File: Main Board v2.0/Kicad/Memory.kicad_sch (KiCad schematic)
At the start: 0 parts

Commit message: update
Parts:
- added C3, C4, C5, C6, C7: 100n, symbol Device:C
- added R1, R2, R3, R4, R5: 10k, symbol Device:R_Small
- added U10, U11, U12, U?: UM61512A, Footprints:DIP-32_0_ELL, symbol Z80-CPU-Board-rescue:UM61512A
- added U9: AM29F040B, Package_DIP:DIP-32_W15.24mm, symbol Memory_RAM:AS6C4008-55PCN
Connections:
- new net: R3.1, U10.30 (CE2)
- new net: R1.1, U?.30 (CE2)
- new net: R5.1, U12.30 (CE2)
- new net: R2.1, U9.31 (WE#)
- new net: R4.1, U11.30 (CE2)
- new net +5V: C3.1, C4.1, C5.1, C6.1, C7.1, R1.2, R2.2, R3.2, R4.2, R5.2, U10.32 (VCC), U11.32 (VCC), U12.32 (VCC), U9.32 (VCC), U?.32 (VCC)
- new net D0: U10.13 (D0), U11.13 (D0), U12.13 (D0), U9.13 (DQ0), U?.13 (D0)
- new net D1: U10.14 (D1), U11.14 (D1), U12.14 (D1), U9.14 (DQ1), U?.14 (D1)
- new net D2: U10.15 (D2), U11.15 (D2), U12.15 (D2), U9.15 (DQ2), U?.15 (D2)
- new net D3: U10.17 (D3), U11.17 (D3), U12.17 (D3), U9.17 (DQ3), U?.17 (D3)
- new net D4: U10.18 (D4), U11.18 (D4), U12.18 (D4), U9.18 (DQ4), U?.18 (D4)
- new net D5: U10.19 (D5), U11.19 (D5), U12.19 (D5), U9.19 (DQ5), U?.19 (D5)
- new net D6: U10.20 (D6), U11.20 (D6), U12.20 (D6), U9.20 (DQ6), U?.20 (D6)
- new net D7: U10.21 (D7), U11.21 (D7), U12.21 (D7), U9.21 (DQ7), U?.21 (D7)
- new net GND: C3.2, C4.2, C5.2, C6.2, C7.2, U10.16 (GND), U11.16 (GND), U12.16 (GND), U9.16 (VSS), U?.16 (GND)
- new net MA0: U10.12 (A0), U11.12 (A0), U12.12 (A0), U9.12 (A0), U?.12 (A0)
- new net MA1: U10.11 (A1), U11.11 (A1), U12.11 (A1), U9.11 (A1), U?.11 (A1)
- new net MA10: U10.23 (A10), U11.23 (A10), U12.23 (A10), U9.23 (A10), U?.23 (A10)
- new net MA11: U10.25 (A11), U11.25 (A11), U12.25 (A11), U9.25 (A11), U?.25 (A11)
- new net MA12: U10.4 (A12), U11.4 (A12), U12.4 (A12), U9.4 (A12), U?.4 (A12)
- new net MA13: U10.28 (A13), U11.28 (A13), U12.28 (A13), U9.28 (A13), U?.28 (A13)
- new net MA14: U10.3 (A14), U11.3 (A14), U12.3 (A14), U?.3 (A14)
- new net MA15: U10.31 (A15), U11.31 (A15), U12.31 (A15), U?.31 (A15)
- new net MA2: U10.10 (A2), U11.10 (A2), U12.10 (A2), U9.10 (A2), U?.10 (A2)
- new net MA3: U10.9 (A3), U11.9 (A3), U12.9 (A3), U9.9 (A3), U?.9 (A3)
- new net MA4: U10.8 (A4), U11.8 (A4), U12.8 (A4), U9.8 (A4), U?.8 (A4)
- new net MA5: U10.7 (A5), U11.7 (A5), U12.7 (A5), U9.7 (A5), U?.7 (A5)
- new net MA6: U10.6 (A6), U11.6 (A6), U12.6 (A6), U9.6 (A6), U?.6 (A6)
- new net MA7: U10.5 (A7), U11.5 (A7), U12.5 (A7), U9.5 (A7), U?.5 (A7)
- new net MA8: U10.27 (A8), U11.27 (A8), U12.27 (A8), U9.27 (A8), U?.27 (A8)
- new net MA9: U10.26 (A9), U11.26 (A9), U12.26 (A9), U9.26 (A9), U?.26 (A9)
- new net MROM_SEL0: U9.29 (A14)
- new net MROM_SEL1: U9.3 (A15)
- new net MROM_SEL2: U9.2 (A16)
- new net MROM_SEL3: U9.30 (A17)
- new net MROM_SEL4: U9.1 (A18)
- new net ~{ME0}: U9.22 (CE#)
- new net ~{ME1}: U11.22 (CE1)
- new net ~{ME2}: U?.22 (CE1)
- new net ~{ME3}: U10.22 (CE1)
- new net ~{ME4}: U12.22 (CE1)
- new net ~{RD}: U10.24 (OE), U11.24 (OE), U12.24 (OE), U9.24 (OE#), U?.24 (OE)
- new net ~{WR}: U10.29 (WR), U11.29 (WR), U12.29 (WR), U?.29 (WR)
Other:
- note added: "ROM has 32x 16k pages."
- note added: "ZIF socket"

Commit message: schematic done*
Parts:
- removed C5, C6, C7: 100n, symbol Device:C
- removed R1, R2, R3, R4, R5: 10k, symbol Device:R_Small
- removed U10, U11, U12, U?: UM61512A, Footprints:DIP-32_0_ELL, symbol Z80-CPU-Board-rescue:UM61512A
- added U5: AS6C4008-55PCN, Package_SO:SOP-32_11.305x20.495mm_P1.27mm, symbol Memory_RAM:AS6C4008-55PCN
- C7: renamed from C3; footprint (none) -> Capacitor_SMD:C_0603_1608Metric_Pad1.08x0.95mm_HandSolder
- C8: renamed from C4; footprint (none) -> Capacitor_SMD:C_0603_1608Metric_Pad1.08x0.95mm_HandSolder
- U6: renamed from U9; footprint Package_DIP:DIP-32_W15.24mm -> Socket:3M_Textool_240-1288-00-0602J_2x20_P2.54mm
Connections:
- net MROM_SEL0 is gone; now on net MA14: U6.29 (A14)
- net MROM_SEL1 is gone; now on net MA15: U6.3 (A15)
- net MROM_SEL2 is gone; now on net MA16: U6.2 (A16)
- net MROM_SEL3 is gone; now on net MA17: U6.30 (A17)
- net MROM_SEL4 is gone; now on net MA18: U6.1 (A18)
- net +5V: now also U5.32 (VCC)
- net D0: now also U5.13 (DQ0)
- net D1: now also U5.14 (DQ1)
- net D2: now also U5.15 (DQ2)
- net D3: now also U5.17 (DQ3)
- net D4: now also U5.18 (DQ4)
- net D5: now also U5.19 (DQ5)
- net D6: now also U5.20 (DQ6)
- net D7: now also U5.21 (DQ7)
- net GND: now also U5.16 (VSS)
- net MA13: now also U5.28 (A13)
- net MA14: now also U5.3 (A14)
- net MA15: now also U5.31 (A15)
- net MA16: now also U5.2 (A16)
- net MA17: now also U5.30 (A17)
- net MA18: now also U5.1 (A18)
- net ROM_WE#: now reaches U6.31 (WE#)
- net MA0 renamed A0
- net A0: now also U5.12 (A0)
- net MA1 renamed A1
- net A1: now also U5.11 (A1)
- net MA10 renamed A10
- net A10: now also U5.23 (A10)
- net MA11 renamed A11
- net A11: now also U5.25 (A11)
- net MA12 renamed A12
- net A12: now also U5.4 (A12)
- net MA2 renamed A2
- net A2: now also U5.10 (A2)
- net MA3 renamed A3
- net A3: now also U5.9 (A3)
- net MA4 renamed A4
- net A4: now also U5.8 (A4)
- net MA5 renamed A5
- net A5: now also U5.7 (A5)
- net MA6 renamed A6
- net A6: now also U5.6 (A6)
- net MA7 renamed A7
- net A7: now also U5.5 (A7)
- net MA8 renamed A8
- net A8: now also U5.27 (A8)
- net MA9 renamed A9
- net A9: now also U5.26 (A9)
- net ~{ME0} renamed ~{ROM_CE}
- net ~{RD} renamed ~{CPU_RD}
- net ~{CPU_RD}: now also U5.24 (OE#)
- new net ~{CPU_WR}: U5.29 (WE#)
- new net ~{RAM_CE}: U5.22 (CE#)
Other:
- note added: "To CPU Sheet"
- note added: "ZIF32 socket"
- note removed: "ROM has 32x 16k pages."
- note removed: "ZIF socket"
- moved on the sheet: U6

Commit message: board update
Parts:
- U6: footprint Socket:3M_Textool_240-1288-00-0602J_2x20_P2.54mm -> Socket:3M_Textool_232-1288-00-0602J_2x16_P2.54mm
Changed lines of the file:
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@@
 	)
 	(hierarchical_label "A[0..15]"
-		(shape input)
+		(shape tri_state)
 		(at 25.4 125.73 180)
 		(effects
@@
 			)
 		)
-		(property "Footprint" "Socket:3M_Textool_240-1288-00-0602J_2x20_P2.54mm"
+		(property "Footprint" "Socket:3M_Textool_232-1288-00-0602J_2x16_P2.54mm"
 			(at 176.53 62.23 0)
 			(hide yes)

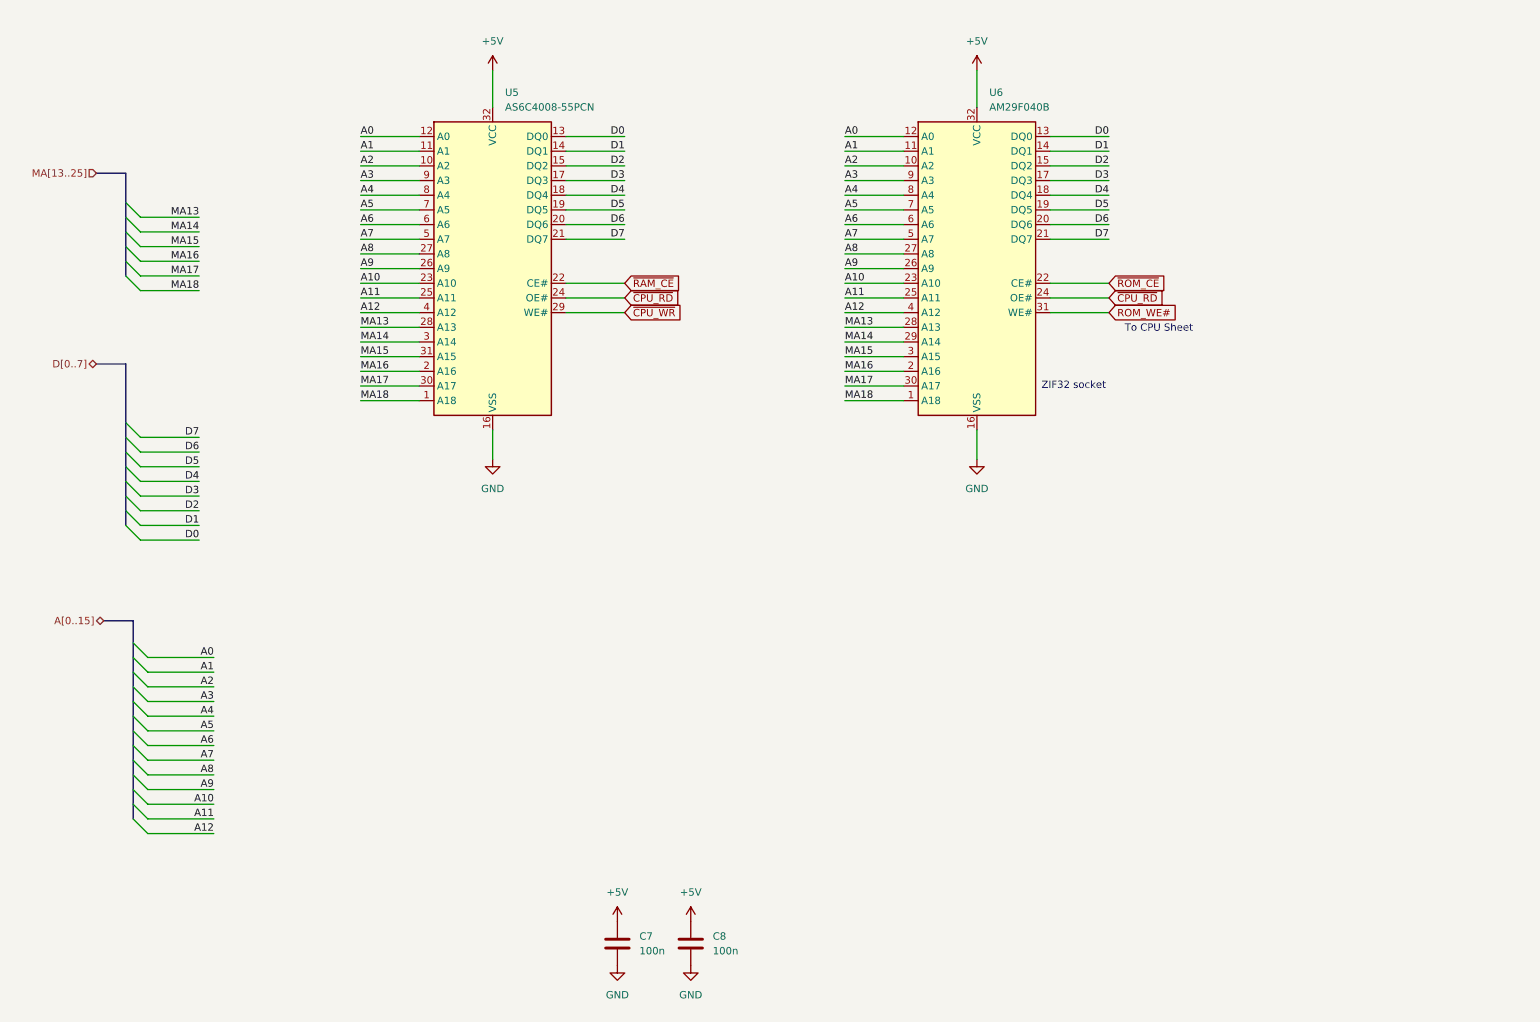
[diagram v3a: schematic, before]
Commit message: schematic update
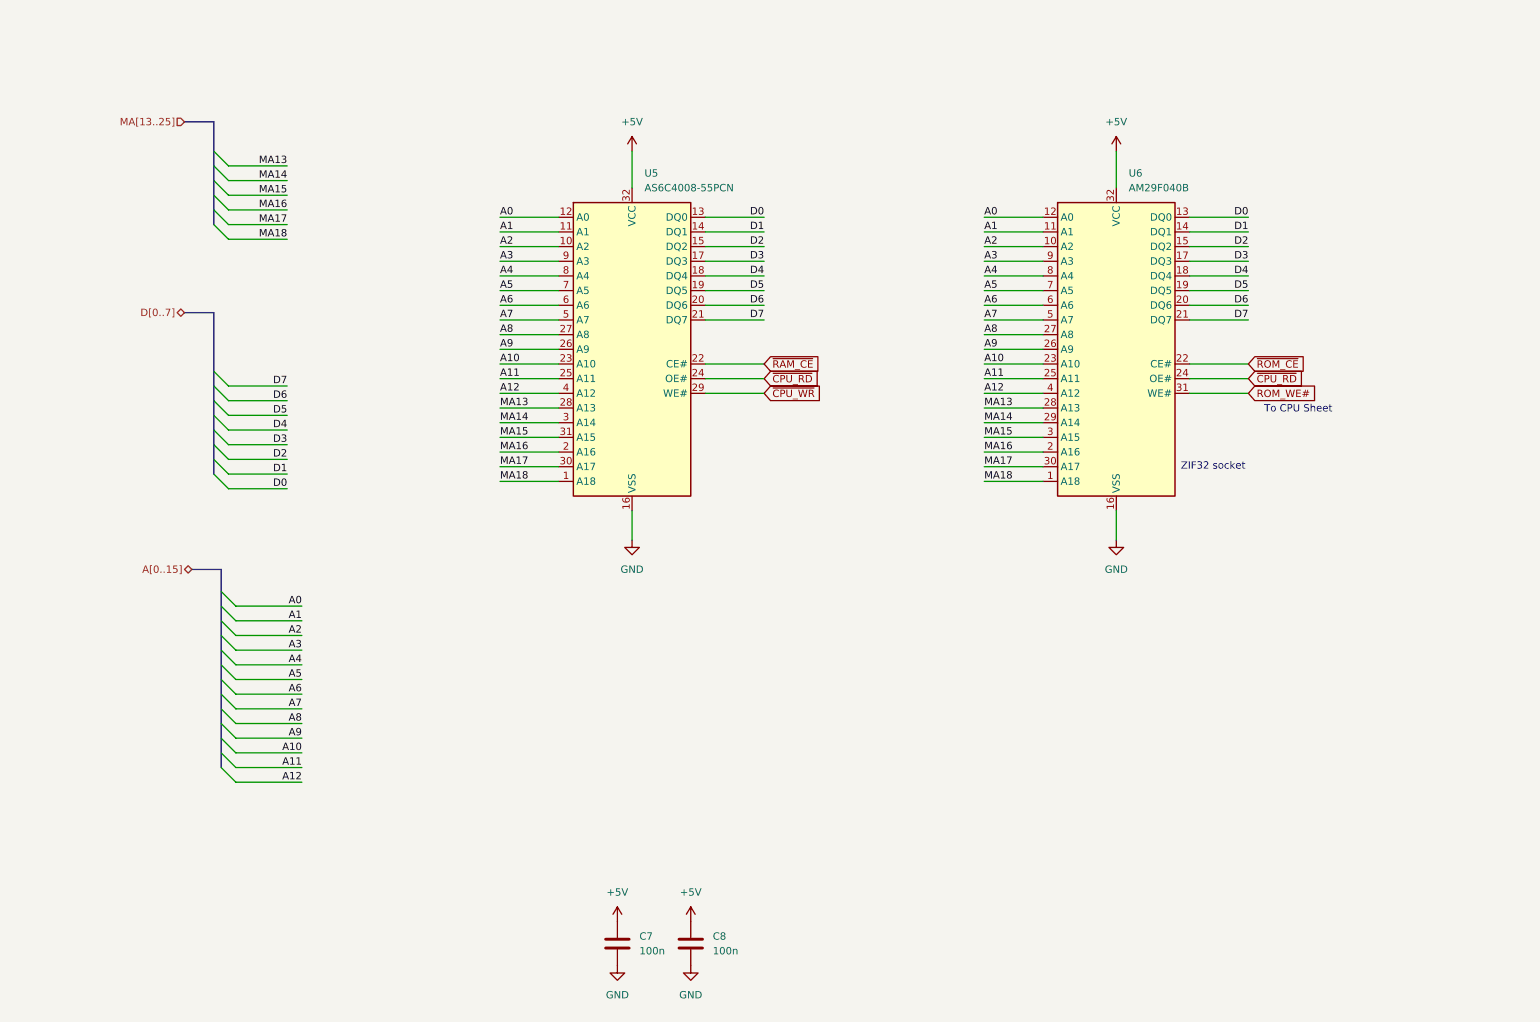
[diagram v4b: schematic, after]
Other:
- moved on the sheet: U5, U6

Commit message: schematic updates
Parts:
- added R27: 10k, Resistor_SMD:R_0603_1608Metric_Pad0.98x0.95mm_HandSolder, symbol Device:R_Small
- renumbered C7 to C5, C8 to C6
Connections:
- net +5V: now also R27.1
- net ROM_WE#: no longer names the net of U6.31 (WE#)
- net ROM_WE#: now also R27.2
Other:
- note removed: "To CPU Sheet"
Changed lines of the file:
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@@
 	(generator_version "10.0")
 	(paper "A4")
-	(text "To CPU Sheet"
-		(exclude_from_sim no)
-		(at 232.156 89.154 0)
-		(effects
-			(font
-				(size 1.27 1.27)
-			)
-		)
-	)
 	(text "ZIF32 socket"
 		(exclude_from_sim no)
@@
 		)
 	)
+	(wire
+		(pts
+			(xy 243.84 77.47) (xy 243.84 80.01)
+		)
+		(stroke
+			(width 0)
+			(type default)
+		)
+	)
 	(bus
 		(pts
@@
 	(wire
 		(pts
+			(xy 243.84 86.36) (xy 243.84 85.09)
+		)
+		(stroke
+			(width 0)
+			(type default)
+		)
+	)
+	(wire
+		(pts
 			(xy 48.26 148.59) (xy 59.69 148.59)
 		)
@@
 	(wire
 		(pts
-			(xy 213.36 86.36) (xy 223.52 86.36)
+			(xy 213.36 86.36) (xy 243.84 86.36)
 		)
 		(stroke
@@
 		(property "Intersheetrefs" "${INTERSHEET_REFS}"
 			(at 150.2447 86.36 0)
-			(hide yes)
-			(show_name no)
-			(do_not_autoplace no)
-			(effects
-				(font
-					(size 1.27 1.27)
-				)
-				(justify left)
-			)
-		)
-	)
-	(global_label "ROM_WE#"
-		(shape input)
-		(at 223.52 86.36 0)
-		(fields_autoplaced yes)
-		(effects
-			(font
-				(size 1.27 1.27)
-			)
-			(justify left)
-		)
-		(property "Intersheetrefs" "${INTERSHEET_REFS}"
-			(at 235.3951 86.36 0)
 			(hide yes)
 			(show_name no)
@@
 		(dnp no)
 		(fields_autoplaced yes)
-		(property "Reference" "#PWR033"
+		(property "Reference" "#PWR036"
 			(at 114.3 181.61 0)
 			(hide yes)
@@
 			(project "Main Board v2.0"
 				(path "/91a97de0-fe3a-4a53-b587-b32edd62d6f9/0256e416-4ec8-489e-ad65-c3c8e0d7f516"
-					(reference "#PWR033")
+					(reference "#PWR036")
 					(unit 1)
 				)
@@
 		(dnp no)
 		(fields_autoplaced yes)
-		(property "Reference" "C8"
+		(property "Reference" "C6"
 			(at 130.81 180.3399 0)
 			(show_name no)
@@
 			(project "Main Board v2.0"
 				(path "/91a97de0-fe3a-4a53-b587-b32edd62d6f9/0256e416-4ec8-489e-ad65-c3c8e0d7f516"
-					(reference "C8")
+					(reference "C6")
 					(unit 1)
 				)
@@
 		(dnp no)
 		(fields_autoplaced yes)
-		(property "Reference" "#PWR038"
+		(property "Reference" "#PWR035"
 			(at 200.66 118.11 0)
 			(hide yes)
@@
 			(project "Main Board v2.0"
 				(path "/91a97de0-fe3a-4a53-b587-b32edd62d6f9/0256e416-4ec8-489e-ad65-c3c8e0d7f516"
-					(reference "#PWR038")
+					(reference "#PWR035")
 					(unit 1)
 				)
@@
 		(dnp no)
 		(fields_autoplaced yes)
-		(property "Reference" "#PWR036"
+		(property "Reference" "#PWR039"
 			(at 127 191.77 0)
 			(hide yes)
@@
 			(project "Main Board v2.0"
 				(path "/91a97de0-fe3a-4a53-b587-b32edd62d6f9/0256e416-4ec8-489e-ad65-c3c8e0d7f516"
-					(reference "#PWR036")
+					(reference "#PWR039")
 					(unit 1)
 				)
@@
 		(dnp no)
 		(fields_autoplaced yes)
-		(property "Reference" "#PWR034"
+		(property "Reference" "#PWR038"
 			(at 114.3 191.77 0)
 			(hide yes)
@@
 			(project "Main Board v2.0"
 				(path "/91a97de0-fe3a-4a53-b587-b32edd62d6f9/0256e416-4ec8-489e-ad65-c3c8e0d7f516"
-					(reference "#PWR034")
+					(reference "#PWR038")
+					(unit 1)
+				)
+			)
+		)
+	)
+	(symbol
+		(lib_id "power:+5V")
+		(at 243.84 77.47 0)
+		(unit 1)
+		(body_style 1)
+		(exclude_from_sim no)
+		(in_bom yes)
+		(on_board yes)
+		(in_pos_files yes)
+		(dnp no)
+		(fields_autoplaced yes)
+		(property "Reference" "#PWR033"
+			(at 243.84 81.28 0)
+			(hide yes)
+			(show_name no)
+			(do_not_autoplace no)
+			(effects
+				(font
+					(size 1.27 1.27)
+				)
+			)
+		)
+		(property "Value" "+5V"
+			(at 243.84 72.39 0)
+			(show_name no)
+			(do_not_autoplace no)
+			(effects
+				(font
+					(size 1.27 1.27)
+				)
+			)
+		)
+		(property "Footprint" ""
+			(at 243.84 77.47 0)
+			(hide yes)
+			(show_name no)
+			(do_not_autoplace no)
+			(effects
+				(font
+					(size 1.27 1.27)
+				)
+			)
+		)
+		(property "Datasheet" ""
+			(at 243.84 77.47 0)
+			(hide yes)
+			(show_name no)
+			(do_not_autoplace no)
+			(effects
+				(font
+					(size 1.27 1.27)
+				)
+			)
+		)
+		(property "Description" "Power symbol creates a global label with name \"+5V\""
+			(at 243.84 77.47 0)
+			(hide yes)
+			(show_name no)
+			(do_not_autoplace no)
+			(effects
+				(font
+					(size 1.27 1.27)
+				)
+			)
+		)
+		(pin "1"
+		)
+		(instances
+			(project "Main Board v2.0"
+				(path "/91a97de0-fe3a-4a53-b587-b32edd62d6f9/0256e416-4ec8-489e-ad65-c3c8e0d7f516"
+					(reference "#PWR033")
 					(unit 1)
 				)
@@
 		(dnp no)
 		(fields_autoplaced yes)
-		(property "Reference" "#PWR032"
+		(property "Reference" "#PWR034"
 			(at 116.84 118.11 0)
 			(hide yes)
@@
 			(project "Main Board v2.0"
 				(path "/91a97de0-fe3a-4a53-b587-b32edd62d6f9/0256e416-4ec8-489e-ad65-c3c8e0d7f516"
-					(reference "#PWR032")
+					(reference "#PWR034")
+					(unit 1)
+				)
+			)
+		)
+	)
+	(symbol
+		(lib_id "Device:R_Small")
+		(at 243.84 82.55 0)
+		(unit 1)
+		(body_style 1)
+		(exclude_from_sim no)
+		(in_bom yes)
+		(on_board yes)
+		(in_pos_files yes)
+		(dnp no)
+		(property "Reference" "R27"
+			(at 245.11 81.28 0)
+			(show_name no)
+			(do_not_autoplace no)
+			(effects
+				(font
+					(size 1.016 1.016)
+				)
+				(justify left)
+			)
+		)
+		(property "Value" "10k"
+			(at 245.11 83.82 0)
+			(show_name no)
+			(do_not_autoplace no)
+			(effects
+				(font
+					(size 1.27 1.27)
+				)
+				(justify left)
+			)
+		)
+		(property "Footprint" "Resistor_SMD:R_0603_1608Metric_Pad0.98x0.95mm_HandSolder"
+			(at 243.84 82.55 0)
+			(hide yes)
+			(show_name no)
+			(do_not_autoplace no)
+			(effects
+				(font
+					(size 1.27 1.27)
+				)
+			)
+		)
+		(property "Datasheet" ""
+			(at 243.84 82.55 0)
+			(hide yes)
+			(show_name no)
+			(do_not_autoplace no)
+			(effects
+				(font
+					(size 1.27 1.27)
+				)
+			)
+		)
+		(property "Description" "Resistor, small symbol"
+			(at 243.84 82.55 0)
+			(hide yes)
+			(show_name no)
+			(do_not_autoplace no)
+			(effects
+				(font
+					(size 1.27 1.27)
+				)
+			)
+		)
+		(pin "1"
+		)
+		(pin "2"
+		)
+		(instances
+			(project "Main Board v2.0"
+				(path "/91a97de0-fe3a-4a53-b587-b32edd62d6f9/0256e416-4ec8-489e-ad65-c3c8e0d7f516"
+					(reference "R27")
 					(unit 1)
 				)
@@
 		(dnp no)
 		(fields_autoplaced yes)
-		(property "Reference" "#PWR035"
+		(property "Reference" "#PWR037"
 			(at 127 181.61 0)
 			(hide yes)
@@
 			(project "Main Board v2.0"
 				(path "/91a97de0-fe3a-4a53-b587-b32edd62d6f9/0256e416-4ec8-489e-ad65-c3c8e0d7f516"
-					(reference "#PWR035")
+					(reference "#PWR037")
 					(unit 1)
 				)
@@
 		(dnp no)
 		(fields_autoplaced yes)
-		(property "Reference" "#PWR037"
+		(property "Reference" "#PWR032"
 			(at 200.66 48.26 0)
 			(hide yes)
@@
 			(project "Main Board v2.0"
 				(path "/91a97de0-fe3a-4a53-b587-b32edd62d6f9/0256e416-4ec8-489e-ad65-c3c8e0d7f516"
-					(reference "#PWR037")
+					(reference "#PWR032")
 					(unit 1)
 				)
@@
 		(dnp no)
 		(fields_autoplaced yes)
-		(property "Reference" "C7"
+		(property "Reference" "C5"
 			(at 118.11 180.3399 0)
 			(show_name no)
@@
 			(project "Main Board v2.0"
 				(path "/91a97de0-fe3a-4a53-b587-b32edd62d6f9/0256e416-4ec8-489e-ad65-c3c8e0d7f516"
-					(reference "C7")
+					(reference "C5")
 					(unit 1)
 				)

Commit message: board update
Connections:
- net A12 renamed MA12
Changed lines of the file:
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@@
+	)
+	(bus_entry
+		(at 44.45 41.91)
+		(size 2.54 2.54)
+		(stroke
+			(width 0)
+			(type default)
+		)
 	)
 	(bus_entry
@@
 	)
 	(bus_entry
-		(at 45.72 151.13)
-		(size 2.54 2.54)
-		(stroke
-			(width 0)
-			(type default)
-		)
-	)
-	(bus_entry
 		(at 45.72 135.89)
 		(size 2.54 2.54)
@@
 		)
 	)
+	(bus
+		(pts
+			(xy 45.72 116.84) (xy 45.72 148.59)
+		)
+		(stroke
+			(width 0)
+			(type default)
+		)
+	)
 	(wire
 		(pts
@@
 	(wire
 		(pts
+			(xy 46.99 44.45) (xy 57.15 44.45)
+		)
+		(stroke
+			(width 0)
+			(type default)
+		)
+	)
+	(wire
+		(pts
 			(xy 104.14 76.2) (xy 93.98 76.2)
 		)
@@
 	(wire
 		(pts
-			(xy 48.26 153.67) (xy 59.69 153.67)
-		)
-		(stroke
-			(width 0)
-			(type default)
-		)
-	)
-	(wire
-		(pts
 			(xy 48.26 125.73) (xy 59.69 125.73)
 		)
@@
 		(pts
 			(xy 187.96 55.88) (xy 177.8 55.88)
-		)
-		(stroke
-			(width 0)
-			(type default)
-		)
-	)
-	(bus
-		(pts
-			(xy 45.72 116.84) (xy 45.72 151.13)
 		)
 		(stroke
@@
 		)
 	)
-	(label "A12"
+	(label "MA12"
 		(at 93.98 86.36 0)
 		(effects
@@
 		)
 	)
+	(label "MA12"
+		(at 57.15 44.45 180)
+		(effects
+			(font
+				(size 1.27 1.27)
+			)
+			(justify right bottom)
+		)
+	)
 	(label "A0"
 		(at 59.69 123.19 180)
@@
 		)
 	)
-	(label "A12"
+	(label "MA12"
 		(at 177.8 86.36 0)
 		(effects
@@
 	(label "D3"
 		(at 57.15 95.25 180)
-		(effects
-			(font
-				(size 1.27 1.27)
-			)
-			(justify right bottom)
-		)
-	)
-	(label "A12"
-		(at 59.69 153.67 180)
 		(effects
 			(font
@@
 		)
 	)
-	(hierarchical_label "MA[13..25]"
+	(hierarchical_label "MA[12..24]"
 		(shape input)
 		(at 39.37 39.37 180)

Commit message: board update
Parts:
- C5, C6, R27: KiLib_Generator (none) -> SMD_2terminal_chip_molded
- U5: KiLib_Generator (none) -> package/gullwing
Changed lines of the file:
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@@
+			)
+		)
+		(property "KiLib_Generator" "SMD_2terminal_chip_molded"
+			(at 127 181.61 0)
+			(hide yes)
+			(show_name no)
+			(do_not_autoplace no)
+			(effects
+				(font
+					(size 1.27 1.27)
+				)
 			)
 		)
@@
 			)
 		)
+		(property "KiLib_Generator" "SMD_2terminal_chip_molded"
+			(at 243.84 82.55 0)
+			(hide yes)
+			(show_name no)
+			(do_not_autoplace no)
+			(effects
+				(font
+					(size 1.27 1.27)
+				)
+			)
+		)
 		(pin "1"
 		)
@@
 			)
 		)
+		(property "KiLib_Generator" "SMD_2terminal_chip_molded"
+			(at 114.3 181.61 0)
+			(hide yes)
+			(show_name no)
+			(do_not_autoplace no)
+			(effects
+				(font
+					(size 1.27 1.27)
+				)
+			)
+		)
 		(pin "2"
 		)
@@
 			(at 116.84 78.74 0)
 			(hide yes)
+			(show_name no)
+			(do_not_autoplace no)
+			(effects
+				(font
+					(size 1.27 1.27)
+				)
+			)
+		)
+		(property "KiLib_Generator" "package/gullwing"
+			(at 116.84 78.74 0)
+			(hide yes)

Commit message: board rev a routed
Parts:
- renumbered R27 to R34
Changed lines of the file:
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@@
 		(in_pos_files yes)
 		(dnp no)
-		(property "Reference" "R27"
+		(property "Reference" "R34"
 			(at 245.11 81.28 0)
 			(show_name no)
@@
 			(project "Main Board v2.0"
 				(path "/91a97de0-fe3a-4a53-b587-b32edd62d6f9/0256e416-4ec8-489e-ad65-c3c8e0d7f516"
-					(reference "R27")
+					(reference "R34")
 					(unit 1)
 				)
